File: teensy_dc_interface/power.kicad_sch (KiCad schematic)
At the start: 34 parts, among them U3 AP65211A, U4 AP62200TWU-7, U5 NE5532, U6 NE5532, U7 NE5532, U8 NE5532

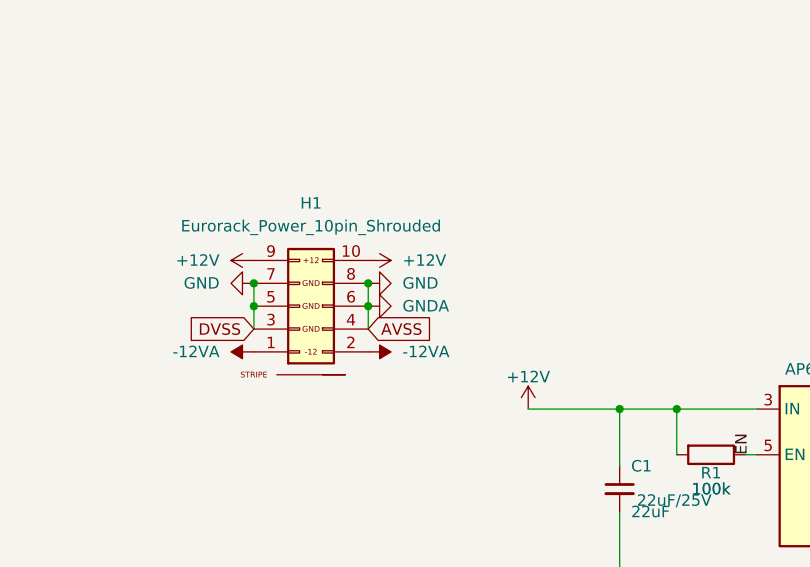
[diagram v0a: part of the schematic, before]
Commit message: teensy to dac connections
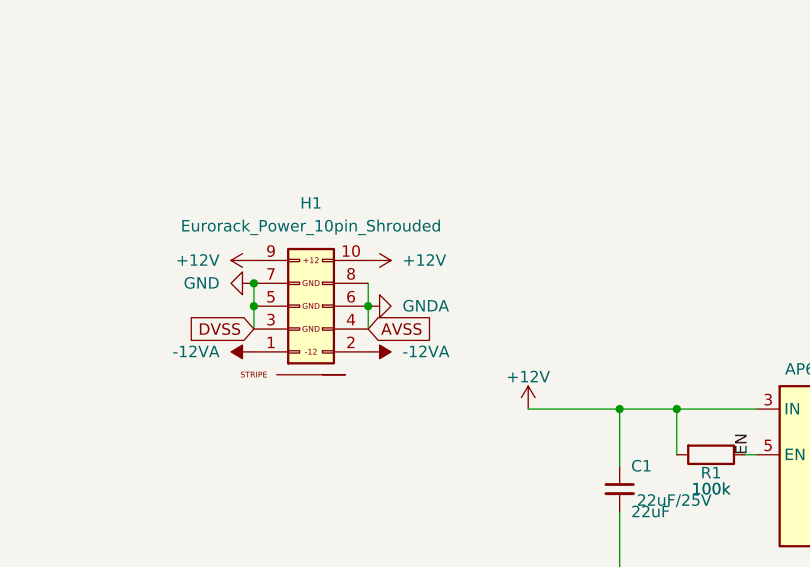
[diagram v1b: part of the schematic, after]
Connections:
- net GND: no longer C1.2, C37.2, C38.2, C39.2, C4.2, C40.1, C41.1, C42.1, C5.2, C6.2, H1.4 (GND), H1.6 (GND), H1.8 (GND), R4.1, U3.1 (GND)
- new net GNDA: C1.2, C37.2, C38.2, C39.2, C4.2, C40.1, C41.1, C42.1, C5.2, C6.2, H1.4 (GND), H1.6 (GND), H1.8 (GND), R4.1, U3.1 (GND)
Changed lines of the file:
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@@
 	)
 	(junction
-		(at 38.1 30.48)
-		(diameter 0)
-		(color 0 0 0 0)
-	)
-	(junction
 		(at 35.56 142.24)
 		(diameter 0)
@@
 					(unit 1)
 				)
-			)
-		)
-	)
-	(symbol
-		(lib_id "4ms_Power-symbol:GND")
-		(at 38.1 30.48 90)
-		(unit 1)
-		(exclude_from_sim no)
-		(in_bom yes)
-		(on_board yes)
-		(dnp no)
-		(property "Reference" "#PWR042"
-			(at 44.45 30.48 0)
-			(effects
-				(font
-					(size 1.27 1.27)
-				)
-				(hide yes)
-			)
-		)
-		(property "Value" "GND"
-			(at 41.91 30.4801 90)
-			(effects
-				(font
-					(size 1.27 1.27)
-				)
-				(justify right)
-			)
-		)
-		(property "Footprint" ""
-			(at 38.1 30.48 0)
-			(effects
-				(font
-					(size 1.27 1.27)
-				)
-				(hide yes)
-			)
-		)
-		(property "Datasheet" ""
-			(at 38.1 30.48 0)
-			(effects
-				(font
-					(size 1.27 1.27)
-				)
-				(hide yes)
-			)
-		)
-		(property "Description" ""
-			(at 38.1 30.48 0)
-			(effects
-				(font
-					(size 1.27 1.27)
-				)
-				(hide yes)
-			)
-		)
-		(pin "1"
-		)
-		(instances
-			(project "teensy_dc_interface"
-				(path "/a4119639-42c9-4d05-afde-5b738907ed5a/1f5c8041-45d6-4a64-aa15-1c1752531f41"
-					(reference "#PWR042")
-					(unit 1)
-				)

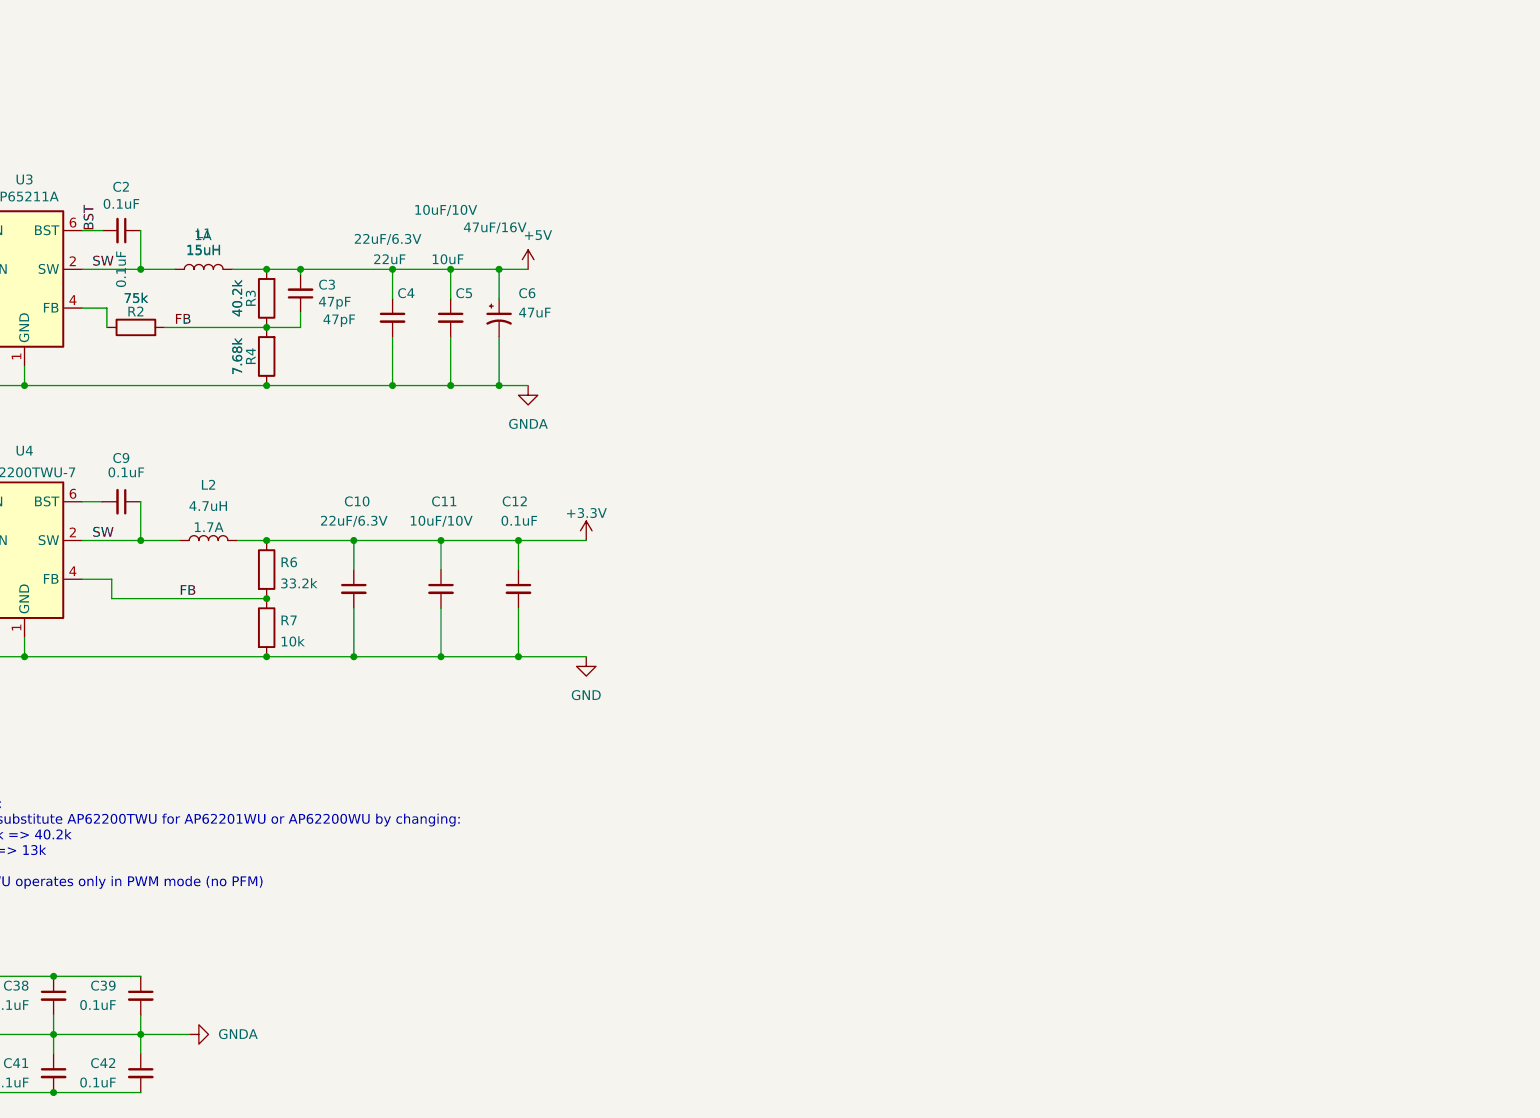
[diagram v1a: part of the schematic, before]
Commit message: Updated filtering between VREF's. Added separate power supply for Teensy on 5V. Added test points. Added ADC input
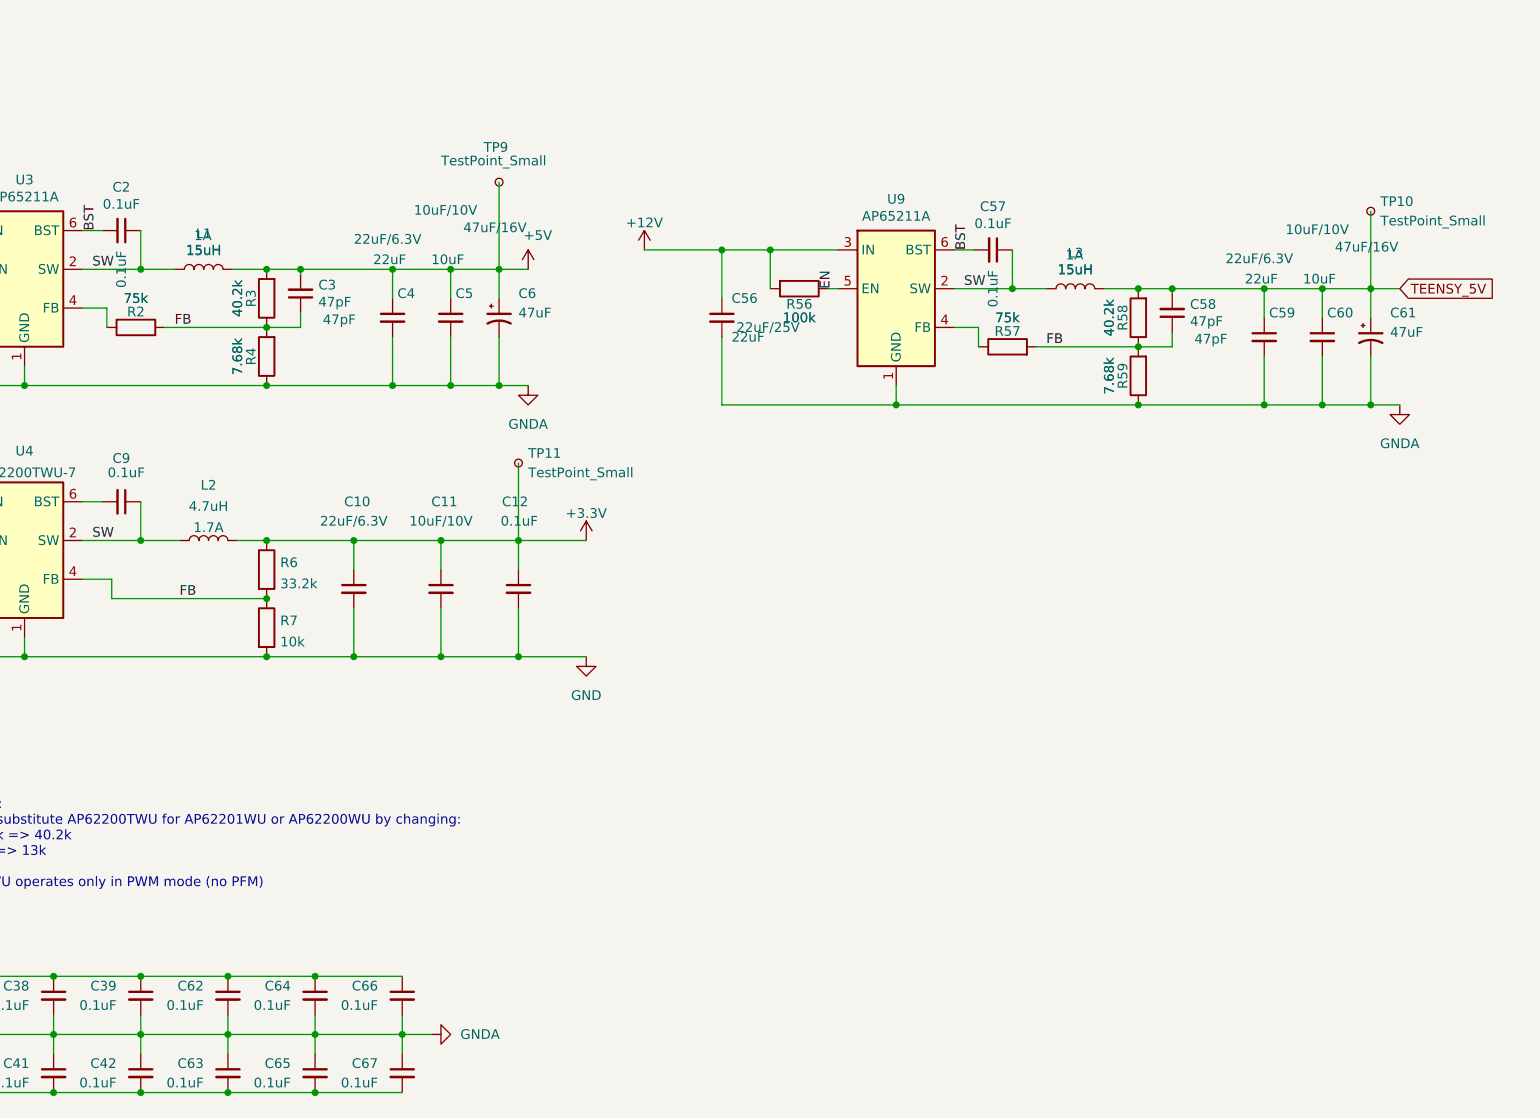
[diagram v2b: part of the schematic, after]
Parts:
- added C56: 22uF, 4ms_Capacitor:C_0805, symbol 4ms_Capacitor:22uF_0805_25V
- added C57: 0.1uF, 4ms_Capacitor:C_0603, symbol 4ms_Capacitor:0.1uF_0603_16V
- added C58: 47pF, 4ms_Capacitor:C_0603, symbol 4ms_Capacitor:47pF_0603_50V
- added C59: 22uF, 4ms_Capacitor:C_0603, symbol 4ms_Capacitor:22uF_0603_6.3V
- added C60: 10uF, 4ms_Capacitor:C_0603, symbol 4ms_Capacitor:10uF_0603_10V
- added C61: 47uF, 4ms_Capacitor:CP_Elec_5x5.3, symbol 4ms_Capacitor:47uF_5x5.3_16V
- added C62, C63, C64, C65, C66, C67: 0.1uF_0603_16V, 4ms_Capacitor:C_0603, symbol 4ms_Capacitor:0.1uF_0603_16V
- added L3: 15uH, 4ms_Inductor:COIL_5040, symbol 4ms_Inductor:15uH_1A_5040
- added R56: 100k, 4ms_Resistor:R_0603, symbol 4ms_Resistor_0603:100k_0603
- added R57: 75k, 4ms_Resistor:R_0603, symbol 4ms_Resistor:75k_0603
- added R58: 40.2k, 4ms_Resistor:R_0603, symbol 4ms_Resistor:40.2k_0603
- added R59: 7.68k, 4ms_Resistor:R_0603, symbol 4ms_Resistor:7.68k_0603
- added TP10, TP11, TP9: TestPoint_Small, TestPoint:TestPoint_Keystone_5005-5009_Compact, symbol 4ms_Connector:TestPoint_Small
- added U9: AP65211A, 4ms_Package_SOT:TSOT-23-6, symbol 4ms_IC:AP65211AWU-7
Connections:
- net +12V: now also C56.1, C63.2, C65.2, C67.2, R56.2, U9.3 (IN)
- net +3.3V: now also TP11.1
- net +5V: now also TP9.1
- net -12VA: now also C62.1, C64.1, C66.1
- net BST: now also C57.2, U9.6 (BST)
- net EN: now also R56.1, U9.5 (EN)
- net FB: now also C58.1, R57.2, R58.1, R59.2
- net GNDA: now also C56.2, C59.2, C60.2, C61.2, C62.2, C63.1, C64.2, C65.1, C66.2, C67.1, R59.1, U9.1 (GND)
- net SW: now also C57.1, L3.1, U9.2 (SW)
- new net: R57.1, U9.4 (FB)
- new net TEENSY_5V: C58.2, C59.1, C60.1, C61.1, L3.2, R58.2, TP10.1

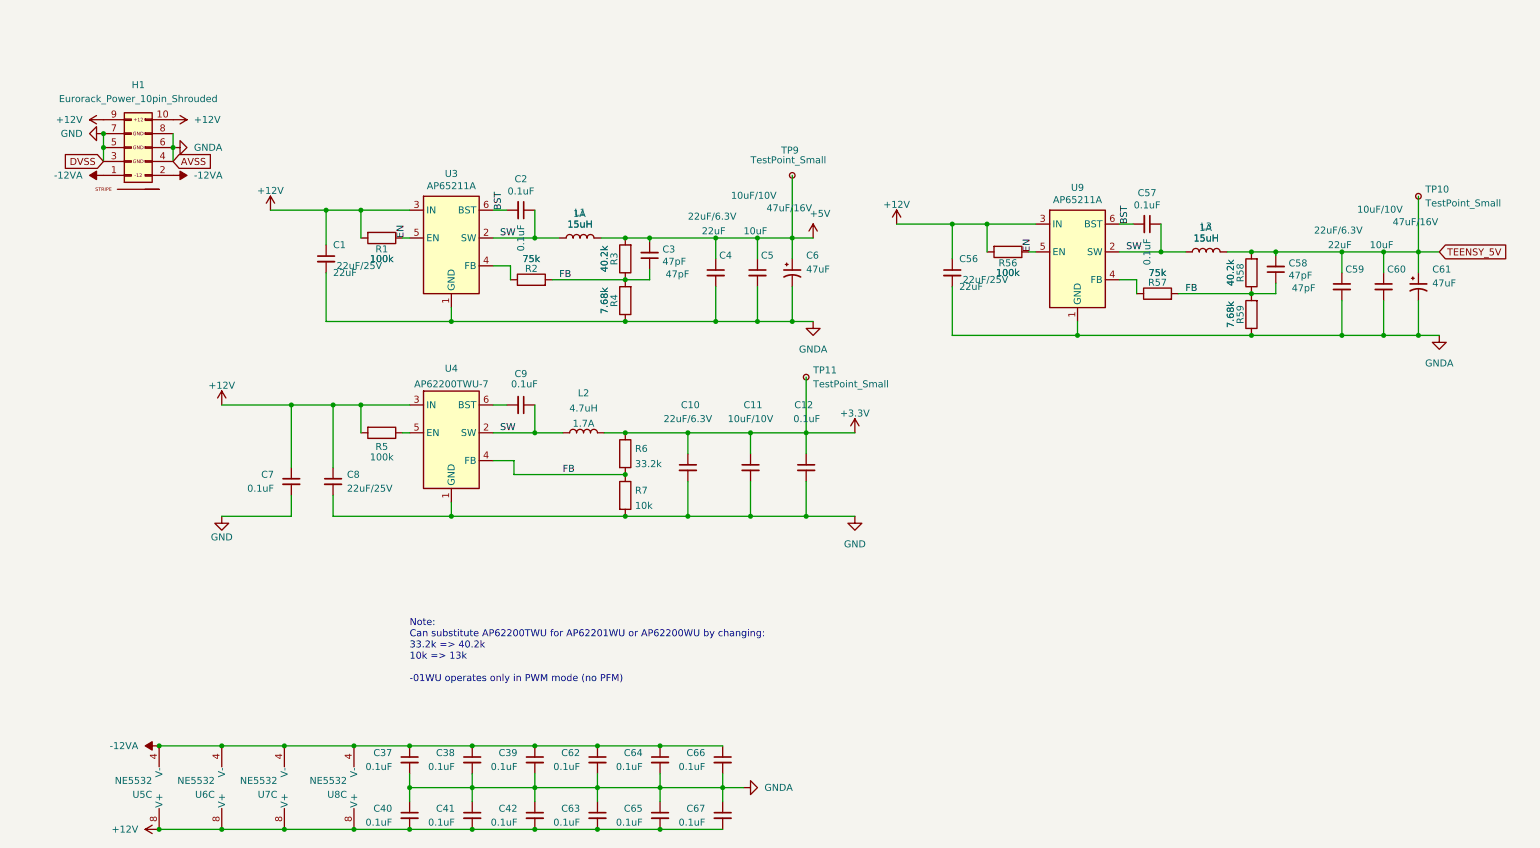
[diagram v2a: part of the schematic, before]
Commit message: out pairs as pages
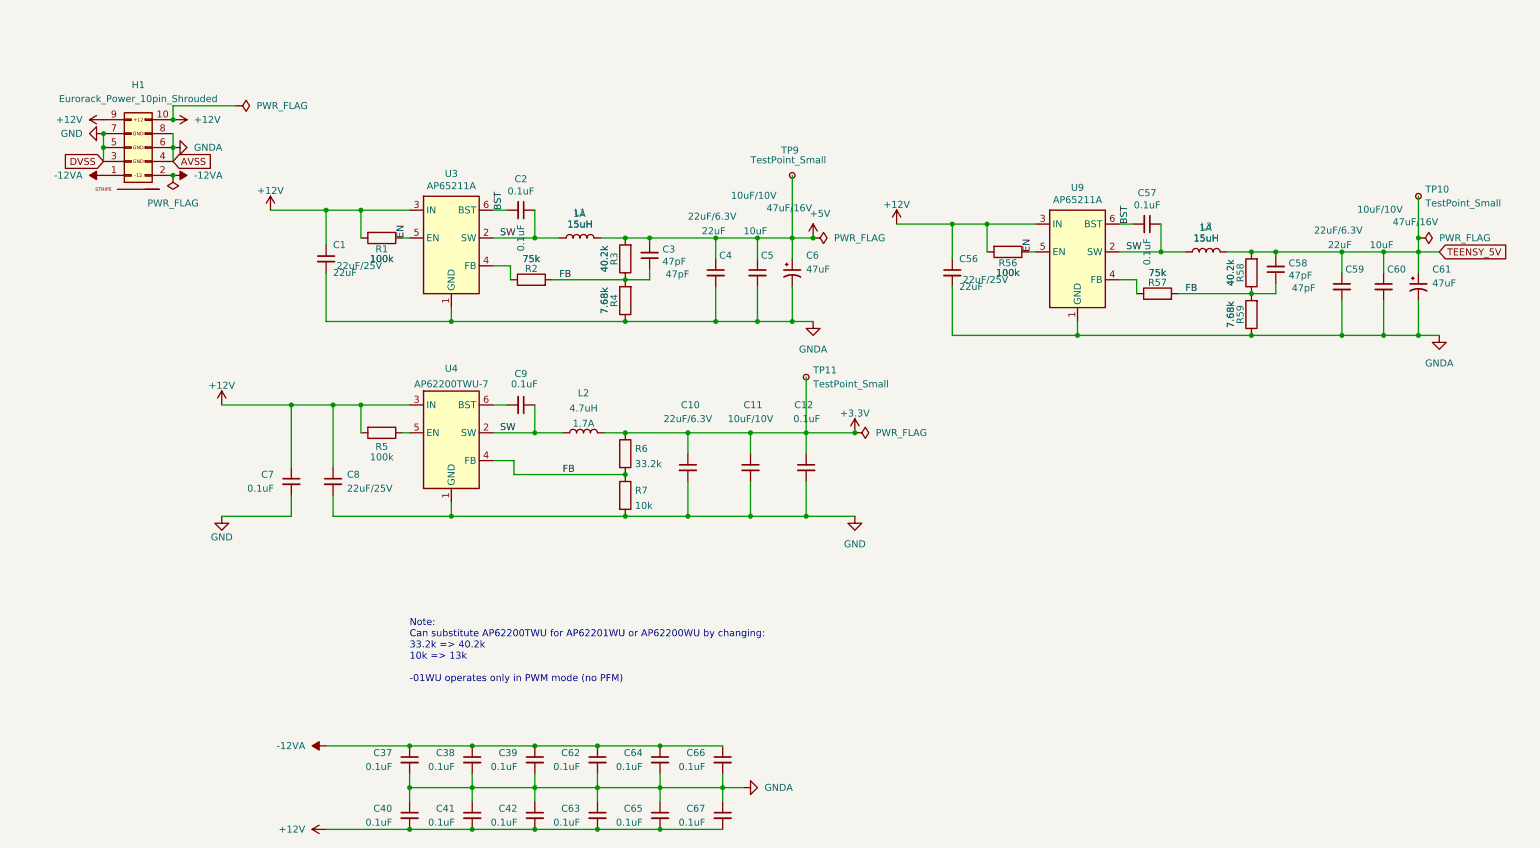
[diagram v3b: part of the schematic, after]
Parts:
- removed U5, U6, U7, U8: NE5532, NE5532DR:SOIC127P599X175-8N, symbol Amplifier_Operational:NE5532
